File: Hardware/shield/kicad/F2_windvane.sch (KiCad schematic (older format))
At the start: 8 parts, among them U301 LMV358

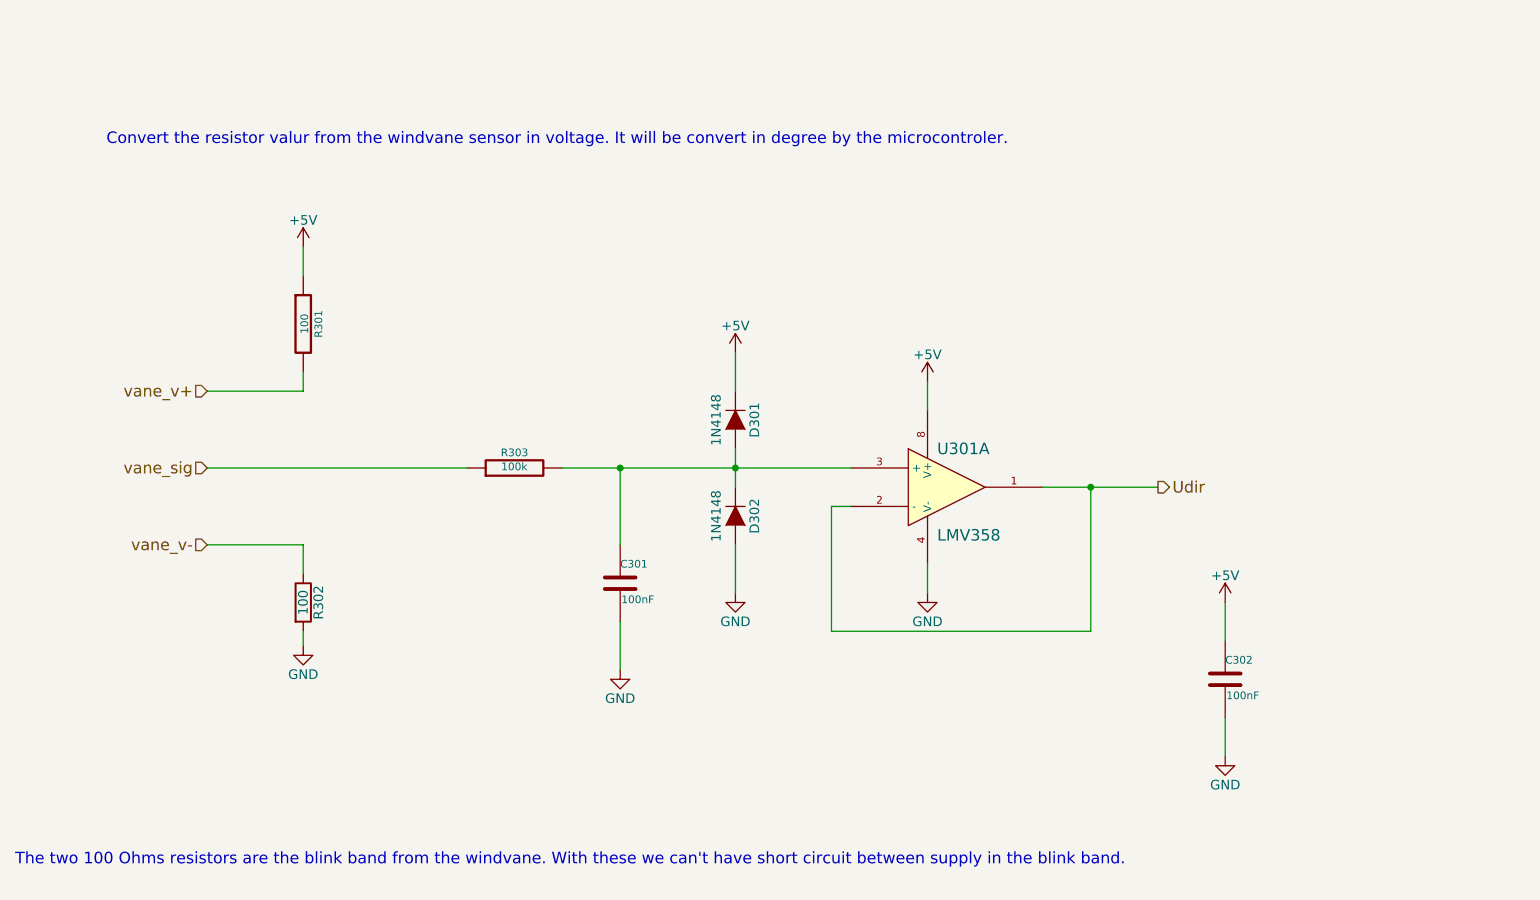
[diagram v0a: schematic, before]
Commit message: Update shield to 2.0.0
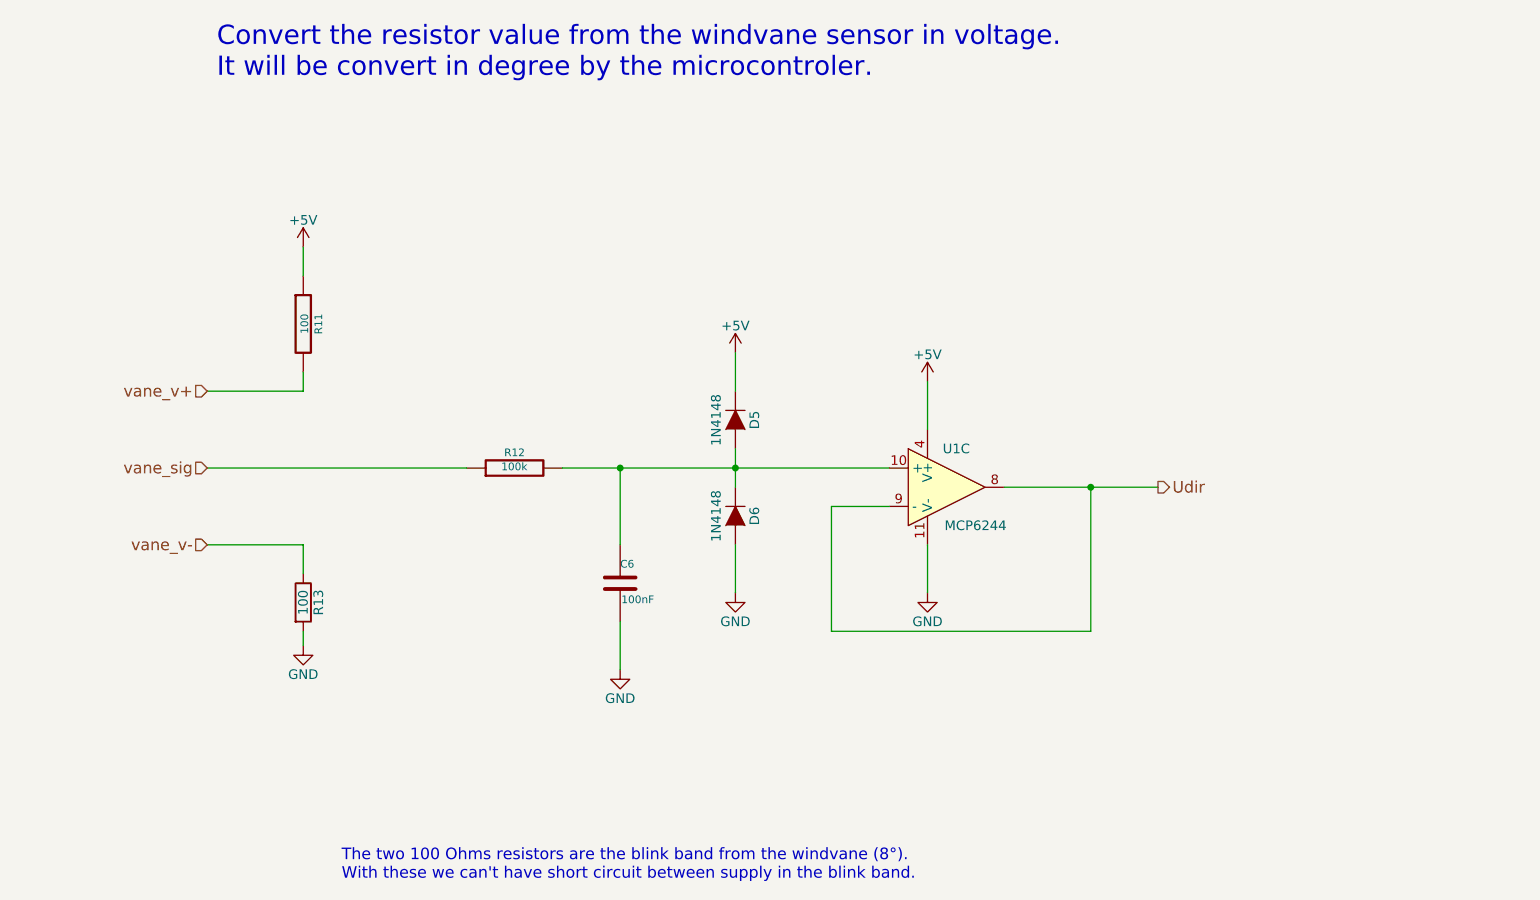
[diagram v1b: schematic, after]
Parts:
- removed C302: 100nF, Capacitors_ThroughHole:C_Rect_L7_W2.5_P5, symbol C-RESCUE-Windlogger
- removed U301: LMV358, Housings_DIP:DIP-8_W7.62mm_LongPads, symbol LM358-RESCUE-Windlogger
- added U1: MCP6244, Housings_DIP:DIP-14_W7.62mm_LongPads, symbol MCP6004
- D5: renamed from D301; footprint Diodes_ThroughHole:Diode_DO-35_SOD27_Horizontal_RM10 -> Discret:DO-35
- D6: renamed from D302; footprint Diodes_ThroughHole:Diode_DO-35_SOD27_Horizontal_RM10 -> Discret:DO-35
- R11: renamed from R301; footprint Discret:R4 -> Discret:R3-LARGE_PADS
- R12: renamed from R303; footprint Discret:R4 -> Discret:R3-LARGE_PADS
- R13: renamed from R302; footprint Discret:R4 -> Discret:R3-LARGE_PADS
- renumbered C301 to C6
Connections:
- net +5V: now also U1.4 (V+)
- net GND: now also U1.11 (V-)
- net Udir: now also U1.8, U1.9 (-)
- net at C6.1, D5.2 (A), D6.1 (K)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: now also U1.10 (+)
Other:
- note added: "Convert the resistor value from the windvane sensor in voltage. \nIt will be convert in degree by the microcontroler."
- note added: "The two 100 Ohms resistors are the blink band from the windvane (8°).\nWith these we can't have short circuit between supply in the blink band."
- note removed: "Convert the resistor valur from the windvane sensor in voltage. It will be convert in degree by the microcontroler."
- note removed: "The two 100 Ohms resistors are the blink band from the windvane. With these we can't have short circuit between supply in the blink band."
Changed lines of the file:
@@
 $Descr A4 11693 8268
 encoding utf-8
-Sheet 3 6
+Sheet 3 5
 Title "Windvane function"
 Date "2016-10-16"
@@
 $EndDescr
 $Comp
-L R-RESCUE-Windlogger R301
+L R-RESCUE-Windlogger R11
 U 1 1 561261A3
 P 4050 2550
-F 0 "R301" V 4130 2550 40  0000 C CNN
+F 0 "R11" V 4130 2550 40  0000 C CNN
 F 1 "100" V 4057 2551 40  0000 C CNN
-F 2 "Discret:R4" V 3980 2550 30  0001 C CNN
+F 2 "Discret:R3-LARGE_PADS" V 3980 2550 30  0001 C CNN
 F 3 "~" H 4050 2550 30  0000 C CNN
 F 4 "0.125W" V 4050 2550 60  0001 C CNN "Puissance"
@@
 $EndComp
 $Comp
-L C-RESCUE-Windlogger C301
+L C-RESCUE-Windlogger C6
 U 1 1 561264FC
 P 5700 3900
-F 0 "C301" H 5700 4000 40  0000 L CNN
+F 0 "C6" H 5700 4000 40  0000 L CNN
 F 1 "100nF" H 5706 3815 40  0000 L CNN
 F 2 "Capacitors_ThroughHole:C_Rect_L7_W2.5_P5" H 5738 3750 30  0001 C CNN
@@
 	4050 2150 4050 2300
 Wire Wire Line
-	7900 3400 8500 3400
+	7700 3400 8500 3400
 Wire Wire Line
 	5700 3300 5700 3700
@@
 	5700 4350 5700 4100
 Wire Wire Line
-	7300 3000 7300 2850
-Wire Wire Line
-	7300 3800 7300 3950
+	7300 2850 7300 3100
+Wire Wire Line
+	7300 3700 7300 3950
 Text HLabel 8500 3400 2    60   Output ~ 0
 Udir
@@
 vane_sig
 $Comp
-L C-RESCUE-Windlogger C302
-U 1 1 56126B37
-P 8850 4400
-F 0 "C302" H 8850 4500 40  0000 L CNN
-F 1 "100nF" H 8856 4315 40  0000 L CNN
-F 2 "Capacitors_ThroughHole:C_Rect_L7_W2.5_P5" H 8888 4250 30  0001 C CNN
-F 3 "~" H 8850 4400 60  0000 C CNN
-F 4 "25V" H 8850 4400 60  0001 C CNN "Tension"
-	1    8850 4400
-	1    0    0    -1
-$EndComp
-Wire Wire Line
-	8850 4000 8850 4200
-Wire Wire Line
-	8850 4600 8850 4800
-$Comp
-L R-RESCUE-Windlogger R303
+L R-RESCUE-Windlogger R12
 U 1 1 5612799B
 P 5150 3300
-F 0 "R303" V 5230 3300 40  0000 C CNN
+F 0 "R12" V 5230 3300 40  0000 C CNN
 F 1 "100k" V 5157 3301 40  0000 C CNN
-F 2 "Discret:R4" V 5080 3300 30  0001 C CNN
+F 2 "Discret:R3-LARGE_PADS" V 5080 3300 30  0001 C CNN
 F 3 "~" H 5150 3300 30  0000 C CNN
 F 4 "0.125W" V 5150 3300 60  0001 C CNN "Puissance"
@@
 	3550 3300 4900 3300
 Wire Wire Line
-	5400 3300 6900 3300
+	5400 3300 7100 3300
 Wire Wire Line
 	8150 4150 8150 3400
@@
 vane_v-
 Wire Wire Line
-	6900 3500 6800 3500
+	6800 3500 7100 3500
 Wire Wire Line
 	6800 3500 6800 4150
@@
 	6300 3700 6300 3950
 $Comp
-L LM358-RESCUE-Windlogger U301
-U 1 1 561263BB
-P 7400 3400
-F 0 "U301" H 7350 3600 60  0000 L CNN
-F 1 "LMV358" H 7350 3150 60  0000 L CNN
-F 2 "Housings_DIP:DIP-8_W7.62mm_LongPads" H 7400 3400 60  0001 C CNN
-F 3 "" H 7400 3400 60  0000 C CNN
-	1    7400 3400
-	1    0    0    -1
-$EndComp
-$Comp
-L +5V #PWR031
+L +5V #PWR034
 U 1 1 573BED92
 P 7300 2850
-F 0 "#PWR031" H 7300 2700 50  0001 C CNN
+F 0 "#PWR034" H 7300 2700 50  0001 C CNN
 F 1 "+5V" H 7300 2990 50  0000 C CNN
 F 2 "" H 7300 2850 50  0000 C CNN
@@
 $EndComp
 $Comp
-L +5V #PWR032
-U 1 1 573BEDC7
-P 8850 4000
-F 0 "#PWR032" H 8850 3850 50  0001 C CNN
-F 1 "+5V" H 8850 4140 50  0000 C CNN
-F 2 "" H 8850 4000 50  0000 C CNN
-F 3 "" H 8850 4000 50  0000 C CNN
-	1    8850 4000
-	1    0    0    -1
-$EndComp
-$Comp
-L +5V #PWR033
+L +5V #PWR035
 U 1 1 573D0C26
 P 4050 2150
-F 0 "#PWR033" H 4050 2000 50  0001 C CNN
+F 0 "#PWR035" H 4050 2000 50  0001 C CNN
 F 1 "+5V" H 4050 2290 50  0000 C CNN
 F 2 "" H 4050 2150 50  0000 C CNN
@@
 $EndComp
 $Comp
-L +5V #PWR034
+L +5V #PWR036
 U 1 1 573D0D74
 P 6300 2700
-F 0 "#PWR034" H 6300 2550 50  0001 C CNN
+F 0 "#PWR036" H 6300 2550 50  0001 C CNN
 F 1 "+5V" H 6300 2840 50  0000 C CNN
 F 2 "" H 6300 2700 50  0000 C CNN
@@
 $EndComp
 $Comp
-L R R302
+L R R13
 U 1 1 57E81F25
 P 4050 4000
-F 0 "R302" V 4130 4000 50  0000 C CNN
+F 0 "R13" V 4130 4000 50  0000 C CNN
 F 1 "100" V 4050 4000 50  0000 C CNN
-F 2 "Discret:R4" V 3980 4000 50  0001 C CNN
+F 2 "Discret:R3-LARGE_PADS" V 3980 4000 50  0001 C CNN
 F 3 "" H 4050 4000 50  0000 C CNN
 	1    4050 4000
@@
 Wire Wire Line
 	4050 4150 4050 4150
-Text Notes 3025 1625 0    60   ~ 0
-Convert the resistor valur from the windvane sensor in voltage. It will be convert in degree by the microcontroler.
-Text Notes 2550 5375 0    60   ~ 0
-The two 100 Ohms resistors are the blink band from the windvane. With these we can't have short circuit between supply in the blink band.
-$Comp
-L GND #PWR035
+Text Notes 3600 1275 0    100  ~ 0
+Convert the resistor value from the windvane sensor in voltage. \nIt will be convert in degree by the microcontroler.
+Text Notes 4250 5450 0    60   ~ 0
+The two 100 Ohms resistors are the blink band from the windvane (8°).\nWith these we can't have short circuit between supply in the blink band.
+$Comp
+L GND #PWR037
 U 1 1 58046061
 P 4050 4225
-F 0 "#PWR035" H 4050 3975 50  0001 C CNN
+F 0 "#PWR037" H 4050 3975 50  0001 C CNN
 F 1 "GND" H 4050 4075 50  0000 C CNN
 F 2 "" H 4050 4225 50  0000 C CNN
@@
 	4050 4225 4050 4150
 $Comp
-L GND #PWR036
+L GND #PWR038
 U 1 1 580460B8
 P 5700 4350
-F 0 "#PWR036" H 5700 4100 50  0001 C CNN
+F 0 "#PWR038" H 5700 4100 50  0001 C CNN
 F 1 "GND" H 5700 4200 50  0000 C CNN
 F 2 "" H 5700 4350 50  0000 C CNN
@@
 $EndComp
 $Comp
-L GND #PWR037
+L GND #PWR039
 U 1 1 580460EC
 P 6300 3950
-F 0 "#PWR037" H 6300 3700 50  0001 C CNN
+F 0 "#PWR039" H 6300 3700 50  0001 C CNN
 F 1 "GND" H 6300 3800 50  0000 C CNN
 F 2 "" H 6300 3950 50  0000 C CNN
@@
 $EndComp
 $Comp
-L GND #PWR038
+L GND #PWR040
 U 1 1 58046118
 P 7300 3950
-F 0 "#PWR038" H 7300 3700 50  0001 C CNN
+F 0 "#PWR040" H 7300 3700 50  0001 C CNN
 F 1 "GND" H 7300 3800 50  0000 C CNN
 F 2 "" H 7300 3950 50  0000 C CNN
@@
 $EndComp
 $Comp
-L GND #PWR039
-U 1 1 58046144
-P 8850 4800
-F 0 "#PWR039" H 8850 4550 50  0001 C CNN
-F 1 "GND" H 8850 4650 50  0000 C CNN
-F 2 "" H 8850 4800 50  0000 C CNN
-F 3 "" H 8850 4800 50  0000 C CNN
-	1    8850 4800
-	1    0    0    -1
-$EndComp
-$Comp
-L D D301
+L D D5
 U 1 1 580461AD
 P 6300 3050
-F 0 "D301" H 6300 3150 50  0000 C CNN
+F 0 "D5" H 6300 3150 50  0000 C CNN
 F 1 "1N4148" H 6300 2950 50  0000 C CNN
-F 2 "Diodes_ThroughHole:Diode_DO-35_SOD27_Horizontal_RM10" H 6300 3050 50  0001 C CNN
+F 2 "Discret:DO-35" H 6300 3050 50  0001 C CNN
 F 3 "" H 6300 3050 50  0000 C CNN
 	1    6300 3050
@@
 $EndComp
 $Comp
-L D D302
+L D D6
 U 1 1 58046207
 P 6300 3550
-F 0 "D302" H 6300 3650 50  0000 C CNN
+F 0 "D6" H 6300 3650 50  0000 C CNN
 F 1 "1N4148" H 6300 3450 50  0000 C CNN
-F 2 "Diodes_ThroughHole:Diode_DO-35_SOD27_Horizontal_RM10" H 6300 3550 50  0001 C CNN
+F 2 "Discret:DO-35" H 6300 3550 50  0001 C CNN
 F 3 "" H 6300 3550 50  0000 C CNN
 	1    6300 3550
 	0    1    1    0
 $EndComp
+$Comp
+L MCP6004 U1
+U 3 1 58593AA6
+P 7400 3400
+F 0 "U1" H 7450 3600 50  0000 C CNN
+F 1 "MCP6244" H 7550 3200 50  0000 C CNN
+F 2 "Housings_DIP:DIP-14_W7.62mm_LongPads" H 7350 3500 50  0001 C CNN
+F 3 "" H 7450 3600 50  0000 C CNN
+	3    7400 3400
+	1    0    0    -1
+$EndComp
 $EndSCHEMATC

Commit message: move to digital 1.1.1
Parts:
- removed U1: MCP6244, Housings_DIP:DIP-14_W7.62mm_LongPads, symbol MCP6004
- added C302: 100nF, Capacitors_ThroughHole:C_Rect_L7_W2.5_P5, symbol C-RESCUE-Windlogger
- added U301: LMV358, Housings_DIP:DIP-8_W7.62mm_LongPads, symbol LM358-RESCUE-Windlogger
- D301: renamed from D5; footprint Discret:DO-35 -> Diodes_ThroughHole:Diode_DO-35_SOD27_Horizontal_RM10
- D302: renamed from D6; footprint Discret:DO-35 -> Diodes_ThroughHole:Diode_DO-35_SOD27_Horizontal_RM10
- R301: renamed from R11; footprint Discret:R3-LARGE_PADS -> Discret:R4
- R302: renamed from R13; footprint Discret:R3-LARGE_PADS -> Discret:R4
- R303: renamed from R12; footprint Discret:R3-LARGE_PADS -> Discret:R4
- renumbered C6 to C301
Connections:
- net +5V: now also C302.1, U301.8 (V+)
- net GND: now also C302.2, U301.4 (V-)
- net Udir: now also U301.1, U301.2 (-)
- net at C301.1, D301.2 (A), D302.1 (K)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: now also U301.3 (+)
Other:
- note added: "Convert the resistor valur from the windvane sensor in voltage. It will be convert in degree by the microcontroler."
- note added: "The two 100 Ohms resistors are the blink band from the windvane. With these we can't have short circuit between supply in the blink band."
- note removed: "Convert the resistor value from the windvane sensor in voltage. \nIt will be convert in degree by the microcontroler."
- note removed: "The two 100 Ohms resistors are the blink band from the windvane (8°).\nWith these we can't have short circuit between supply in the blink band."
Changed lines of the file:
@@
 $Descr A4 11693 8268
 encoding utf-8
-Sheet 3 5
+Sheet 3 6
 Title "Windvane function"
 Date "2016-10-16"
@@
 $EndDescr
 $Comp
-L R-RESCUE-Windlogger R11
+L R-RESCUE-Windlogger R301
 U 1 1 561261A3
 P 4050 2550
-F 0 "R11" V 4130 2550 40  0000 C CNN
+F 0 "R301" V 4130 2550 40  0000 C CNN
 F 1 "100" V 4057 2551 40  0000 C CNN
-F 2 "Discret:R3-LARGE_PADS" V 3980 2550 30  0001 C CNN
+F 2 "Discret:R4" V 3980 2550 30  0001 C CNN
 F 3 "~" H 4050 2550 30  0000 C CNN
 F 4 "0.125W" V 4050 2550 60  0001 C CNN "Puissance"
@@
 $EndComp
 $Comp
-L C-RESCUE-Windlogger C6
+L C-RESCUE-Windlogger C301
 U 1 1 561264FC
 P 5700 3900
-F 0 "C6" H 5700 4000 40  0000 L CNN
+F 0 "C301" H 5700 4000 40  0000 L CNN
 F 1 "100nF" H 5706 3815 40  0000 L CNN
 F 2 "Capacitors_ThroughHole:C_Rect_L7_W2.5_P5" H 5738 3750 30  0001 C CNN
@@
 	4050 2150 4050 2300
 Wire Wire Line
-	7700 3400 8500 3400
+	7900 3400 8500 3400
 Wire Wire Line
 	5700 3300 5700 3700
@@
 	5700 4350 5700 4100
 Wire Wire Line
-	7300 2850 7300 3100
-Wire Wire Line
-	7300 3700 7300 3950
+	7300 3000 7300 2850
+Wire Wire Line
+	7300 3800 7300 3950
 Text HLabel 8500 3400 2    60   Output ~ 0
 Udir
@@
 vane_sig
 $Comp
-L R-RESCUE-Windlogger R12
+L C-RESCUE-Windlogger C302
+U 1 1 56126B37
+P 8850 4400
+F 0 "C302" H 8850 4500 40  0000 L CNN
+F 1 "100nF" H 8856 4315 40  0000 L CNN
+F 2 "Capacitors_ThroughHole:C_Rect_L7_W2.5_P5" H 8888 4250 30  0001 C CNN
+F 3 "~" H 8850 4400 60  0000 C CNN
+F 4 "25V" H 8850 4400 60  0001 C CNN "Tension"
+	1    8850 4400
+	1    0    0    -1
+$EndComp
+Wire Wire Line
+	8850 4000 8850 4200
+Wire Wire Line
+	8850 4600 8850 4800
+$Comp
+L R-RESCUE-Windlogger R303
 U 1 1 5612799B
 P 5150 3300
-F 0 "R12" V 5230 3300 40  0000 C CNN
+F 0 "R303" V 5230 3300 40  0000 C CNN
 F 1 "100k" V 5157 3301 40  0000 C CNN
-F 2 "Discret:R3-LARGE_PADS" V 5080 3300 30  0001 C CNN
+F 2 "Discret:R4" V 5080 3300 30  0001 C CNN
 F 3 "~" H 5150 3300 30  0000 C CNN
 F 4 "0.125W" V 5150 3300 60  0001 C CNN "Puissance"
@@
 	3550 3300 4900 3300
 Wire Wire Line
-	5400 3300 7100 3300
+	5400 3300 6900 3300
 Wire Wire Line
 	8150 4150 8150 3400
@@
 vane_v-
 Wire Wire Line
-	6800 3500 7100 3500
+	6900 3500 6800 3500
 Wire Wire Line
 	6800 3500 6800 4150
@@
 	6300 3700 6300 3950
 $Comp
-L +5V #PWR034
+L LM358-RESCUE-Windlogger U301
+U 1 1 561263BB
+P 7400 3400
+F 0 "U301" H 7350 3600 60  0000 L CNN
+F 1 "LMV358" H 7350 3150 60  0000 L CNN
+F 2 "Housings_DIP:DIP-8_W7.62mm_LongPads" H 7400 3400 60  0001 C CNN
+F 3 "" H 7400 3400 60  0000 C CNN
+	1    7400 3400
+	1    0    0    -1
+$EndComp
+$Comp
+L +5V #PWR031
 U 1 1 573BED92
 P 7300 2850
-F 0 "#PWR034" H 7300 2700 50  0001 C CNN
+F 0 "#PWR031" H 7300 2700 50  0001 C CNN
 F 1 "+5V" H 7300 2990 50  0000 C CNN
 F 2 "" H 7300 2850 50  0000 C CNN
@@
 $EndComp
 $Comp
-L +5V #PWR035
+L +5V #PWR032
+U 1 1 573BEDC7
+P 8850 4000
+F 0 "#PWR032" H 8850 3850 50  0001 C CNN
+F 1 "+5V" H 8850 4140 50  0000 C CNN
+F 2 "" H 8850 4000 50  0000 C CNN
+F 3 "" H 8850 4000 50  0000 C CNN
+	1    8850 4000
+	1    0    0    -1
+$EndComp
+$Comp
+L +5V #PWR033
 U 1 1 573D0C26
 P 4050 2150
-F 0 "#PWR035" H 4050 2000 50  0001 C CNN
+F 0 "#PWR033" H 4050 2000 50  0001 C CNN
 F 1 "+5V" H 4050 2290 50  0000 C CNN
 F 2 "" H 4050 2150 50  0000 C CNN
@@
 $EndComp
 $Comp
-L +5V #PWR036
+L +5V #PWR034
 U 1 1 573D0D74
 P 6300 2700
-F 0 "#PWR036" H 6300 2550 50  0001 C CNN
+F 0 "#PWR034" H 6300 2550 50  0001 C CNN
 F 1 "+5V" H 6300 2840 50  0000 C CNN
 F 2 "" H 6300 2700 50  0000 C CNN
@@
 $EndComp
 $Comp
-L R R13
+L R R302
 U 1 1 57E81F25
 P 4050 4000
-F 0 "R13" V 4130 4000 50  0000 C CNN
+F 0 "R302" V 4130 4000 50  0000 C CNN
 F 1 "100" V 4050 4000 50  0000 C CNN
-F 2 "Discret:R3-LARGE_PADS" V 3980 4000 50  0001 C CNN
+F 2 "Discret:R4" V 3980 4000 50  0001 C CNN
 F 3 "" H 4050 4000 50  0000 C CNN
 	1    4050 4000
@@
 Wire Wire Line
 	4050 4150 4050 4150
-Text Notes 3600 1275 0    100  ~ 0
-Convert the resistor value from the windvane sensor in voltage. \nIt will be convert in degree by the microcontroler.
-Text Notes 4250 5450 0    60   ~ 0
-The two 100 Ohms resistors are the blink band from the windvane (8°).\nWith these we can't have short circuit between supply in the blink band.
-$Comp
-L GND #PWR037
+Text Notes 3025 1625 0    60   ~ 0
+Convert the resistor valur from the windvane sensor in voltage. It will be convert in degree by the microcontroler.
+Text Notes 2550 5375 0    60   ~ 0
+The two 100 Ohms resistors are the blink band from the windvane. With these we can't have short circuit between supply in the blink band.
+$Comp
+L GND #PWR035
 U 1 1 58046061
 P 4050 4225
-F 0 "#PWR037" H 4050 3975 50  0001 C CNN
+F 0 "#PWR035" H 4050 3975 50  0001 C CNN
 F 1 "GND" H 4050 4075 50  0000 C CNN
 F 2 "" H 4050 4225 50  0000 C CNN
@@
 	4050 4225 4050 4150
 $Comp
-L GND #PWR038
+L GND #PWR036
 U 1 1 580460B8
 P 5700 4350
-F 0 "#PWR038" H 5700 4100 50  0001 C CNN
+F 0 "#PWR036" H 5700 4100 50  0001 C CNN
 F 1 "GND" H 5700 4200 50  0000 C CNN
 F 2 "" H 5700 4350 50  0000 C CNN
@@
 $EndComp
 $Comp
-L GND #PWR039
+L GND #PWR037
 U 1 1 580460EC
 P 6300 3950
-F 0 "#PWR039" H 6300 3700 50  0001 C CNN
+F 0 "#PWR037" H 6300 3700 50  0001 C CNN
 F 1 "GND" H 6300 3800 50  0000 C CNN
 F 2 "" H 6300 3950 50  0000 C CNN
@@
 $EndComp
 $Comp
-L GND #PWR040
+L GND #PWR038
 U 1 1 58046118
 P 7300 3950
-F 0 "#PWR040" H 7300 3700 50  0001 C CNN
+F 0 "#PWR038" H 7300 3700 50  0001 C CNN
 F 1 "GND" H 7300 3800 50  0000 C CNN
 F 2 "" H 7300 3950 50  0000 C CNN
@@
 $EndComp
 $Comp
-L D D5
+L GND #PWR039
+U 1 1 58046144
+P 8850 4800
+F 0 "#PWR039" H 8850 4550 50  0001 C CNN
+F 1 "GND" H 8850 4650 50  0000 C CNN
+F 2 "" H 8850 4800 50  0000 C CNN
+F 3 "" H 8850 4800 50  0000 C CNN
+	1    8850 4800
+	1    0    0    -1
+$EndComp
+$Comp
+L D D301
 U 1 1 580461AD
 P 6300 3050
-F 0 "D5" H 6300 3150 50  0000 C CNN
+F 0 "D301" H 6300 3150 50  0000 C CNN
 F 1 "1N4148" H 6300 2950 50  0000 C CNN
-F 2 "Discret:DO-35" H 6300 3050 50  0001 C CNN
+F 2 "Diodes_ThroughHole:Diode_DO-35_SOD27_Horizontal_RM10" H 6300 3050 50  0001 C CNN
 F 3 "" H 6300 3050 50  0000 C CNN
 	1    6300 3050
@@
 $EndComp
 $Comp
-L D D6
+L D D302
 U 1 1 58046207
 P 6300 3550
-F 0 "D6" H 6300 3650 50  0000 C CNN
+F 0 "D302" H 6300 3650 50  0000 C CNN
 F 1 "1N4148" H 6300 3450 50  0000 C CNN
-F 2 "Discret:DO-35" H 6300 3550 50  0001 C CNN
+F 2 "Diodes_ThroughHole:Diode_DO-35_SOD27_Horizontal_RM10" H 6300 3550 50  0001 C CNN
 F 3 "" H 6300 3550 50  0000 C CNN
 	1    6300 3550
 	0    1    1    0
 $EndComp
-$Comp
-L MCP6004 U1
-U 3 1 58593AA6
-P 7400 3400
-F 0 "U1" H 7450 3600 50  0000 C CNN
-F 1 "MCP6244" H 7550 3200 50  0000 C CNN
-F 2 "Housings_DIP:DIP-14_W7.62mm_LongPads" H 7350 3500 50  0001 C CNN
-F 3 "" H 7450 3600 50  0000 C CNN
-	3    7400 3400
-	1    0    0    -1
-$EndComp
 $EndSCHEMATC
